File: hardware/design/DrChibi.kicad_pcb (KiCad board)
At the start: 4 copper layers, 143.5 x 14 mm, 255 parts, among them P1 CONN_02X05, P2 PAD_SMD, P3 IN+, P4 IN-, P5 CONN_01X04, U1 STM32F40X_LQFP64, U2 ISO1050, X1 MINI-USB-SHIELD-32005-201, X2 8MHz 10ppm

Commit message: Includex 4 fiducials for easier machine setup
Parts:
- removed REFSYMGNU: Symbol_GNU-Logo_SilkscreenTop, Symbols:Symbol_GNU-Logo_SilkscreenTop
- added REF**: Fiducial_1mm_Dia_2.54mm_Outer_CopperTop, Fiducials:Fiducial_1mm_Dia_2.54mm_Outer_CopperTop, F.Cu at (36.2, 98.1)
- added REF**: Fiducial_1mm_Dia_2.54mm_Outer_CopperTop, Fiducials:Fiducial_1mm_Dia_2.54mm_Outer_CopperTop, F.Cu at (176.4, 97.3)
- added REF**: Fiducial_1mm_Dia_2.54mm_Outer_CopperTop, Fiducials:Fiducial_1mm_Dia_2.54mm_Outer_CopperTop, F.Cu at (36.2, 101.7)
- added REF**: Fiducial_1mm_Dia_2.54mm_Outer_CopperTop, Fiducials:Fiducial_1mm_Dia_2.54mm_Outer_CopperTop, F.Cu at (176.4, 102.7)
- added REF**: Fiducial_1mm_Dia_2.54mm_Outer_CopperBottom, Fiducials:Fiducial_1mm_Dia_2.54mm_Outer_CopperBottom, F.Cu at (36.2, 98.1)
- added REF**: Fiducial_1mm_Dia_2.54mm_Outer_CopperBottom, Fiducials:Fiducial_1mm_Dia_2.54mm_Outer_CopperBottom, F.Cu at (36.2, 101.7)
- added REF**: Fiducial_1mm_Dia_2.54mm_Outer_CopperBottom, Fiducials:Fiducial_1mm_Dia_2.54mm_Outer_CopperBottom, F.Cu at (176.4, 97.3)
- added REF**: Fiducial_1mm_Dia_2.54mm_Outer_CopperBottom, Fiducials:Fiducial_1mm_Dia_2.54mm_Outer_CopperBottom, F.Cu at (176.4, 102.7)
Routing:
- net GND: track 948.4 -> 950.1 mm

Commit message: Included option for filtering sensev through small caps on RYSx
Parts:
- removed the REF** at (36.2, 98.1) (x2)
- removed the REF** at (176.4, 102.7) (x2)
- added RYSGND1: 0R/DNP, Resistors_SMD:R_0603_HandSoldering, B.Cu at (68.8, 101.3)
- moved REF** 1.78 mm to (36.2, 99.9) (x2)
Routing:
- net GND: track 950.1 -> 959.2 mm
- net /MCU/SENSVY2: track 13.3 -> 20.0 mm

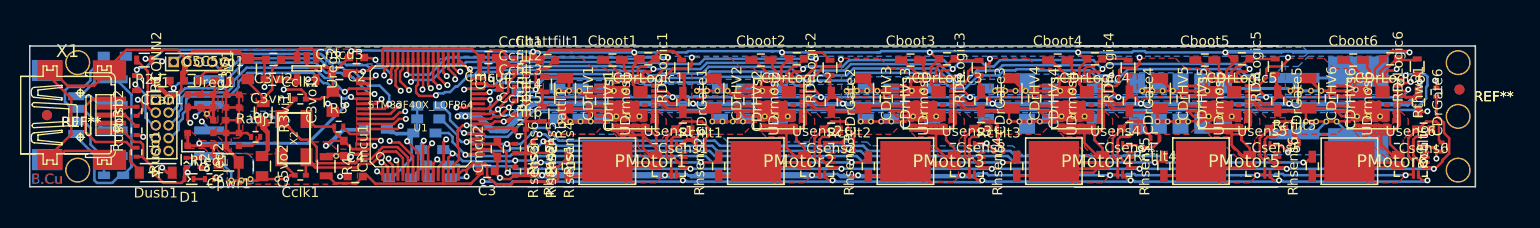
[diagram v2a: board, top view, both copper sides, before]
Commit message: Fixed footprint CDrHV1back6. Made a few things a little bit nicer.
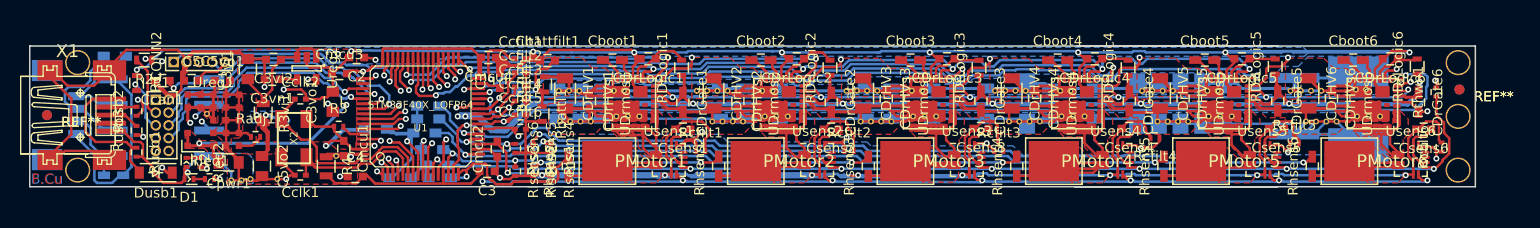
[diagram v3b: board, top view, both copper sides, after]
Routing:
- net GND: track 959.2 -> 1036.8 mm
- net +24V: track 240.0 -> 305.6 mm
- net /Half Bridge A/ZCD_EN: track 109.6 -> 110.8 mm
- net /Half Bridge D/PWM: track 71.5 -> 72.6 mm
- net /Half Bridge C/PWM: track 62.2 -> 63.1 mm
- net /Half Bridge E/PWM: track 84.1 -> 83.5 mm

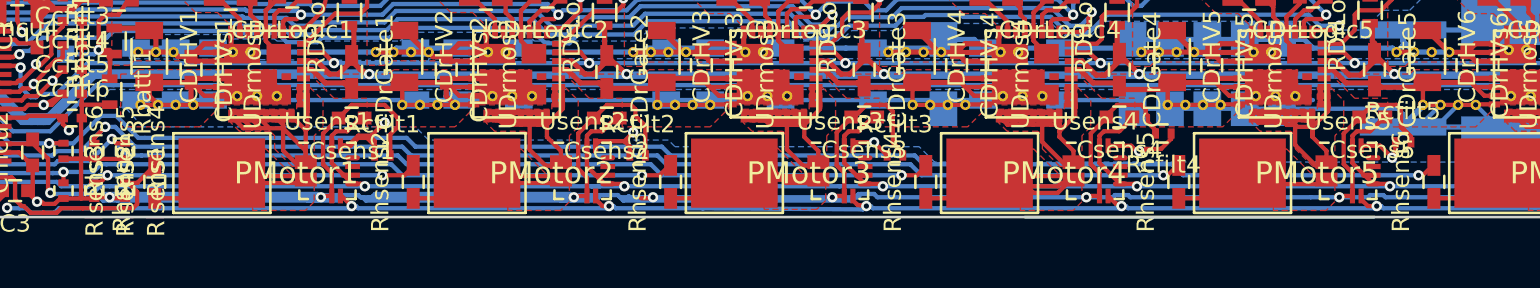
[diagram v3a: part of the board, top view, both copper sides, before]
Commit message: Added pads PVsensx for the application of alterate voltage sensing probes.
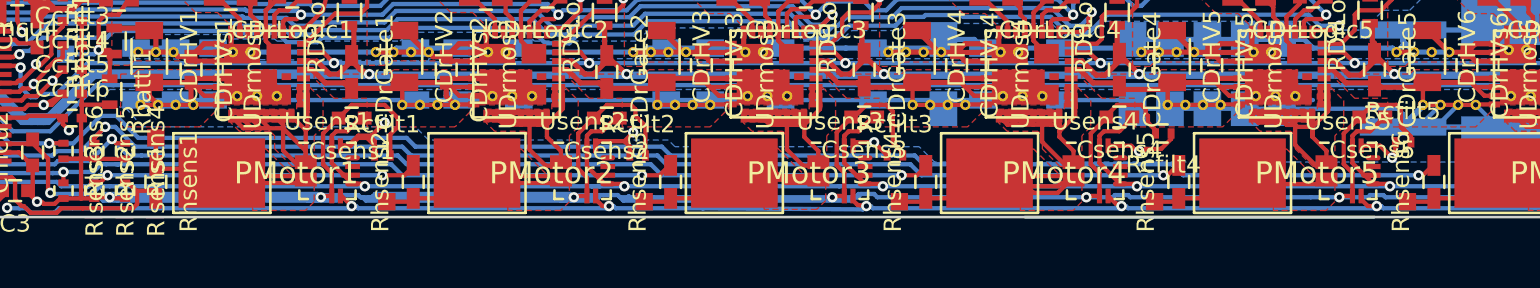
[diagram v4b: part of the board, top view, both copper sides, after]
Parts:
- added PVSens1: PAD_SMD, Pads:PAD_SMD_1x1, F.Cu at (88.0, 102.4)
- added PVSens2: PAD_SMD, Pads:PAD_SMD_1x1, F.Cu at (101.4, 106.1)
- added PVSens3: PAD_SMD, Pads:PAD_SMD_1x1, F.Cu at (116.2, 106.1)
- added PVSens4: PAD_SMD, Pads:PAD_SMD_1x1, F.Cu at (130.9, 106.1)
- added PVSens5: PAD_SMD, Pads:PAD_SMD_1x1, F.Cu at (145.7, 106.1)
- added PVSens6: PAD_SMD, Pads:PAD_SMD_1x1, F.Cu at (160.3, 106.1)
- moved Rhsens1 0.06 mm to (88.0, 105.0), turned to 270 degrees
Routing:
- net Net-(PMotor1-Pad1): track 16.9 -> 20.5 mm
- net Net-(PMotor4-Pad1): track 20.0 -> 21.6 mm
- net Net-(PMotor2-Pad1): track 14.8 -> 16.4 mm
- net Net-(PMotor3-Pad1): track 23.9 -> 25.5 mm
- net Net-(PMotor6-Pad1): track 14.3 -> 15.9 mm
- net Net-(PMotor5-Pad1): track 9.59 -> 11.1 mm
- net GND: track 1036.8 -> 1036.0 mm, vias 25 -> 24
- net /Virtual Y/SENS1: track 17.9 -> 17.2 mm

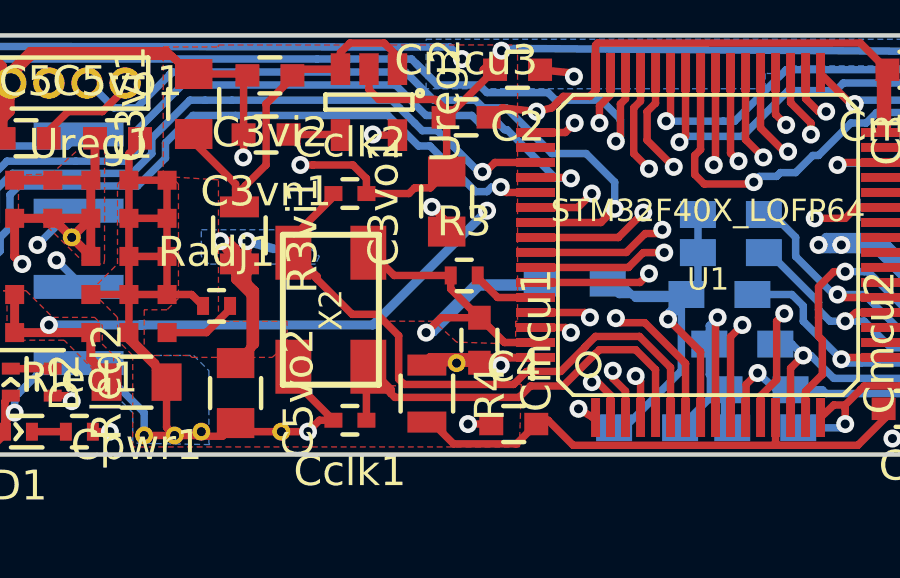
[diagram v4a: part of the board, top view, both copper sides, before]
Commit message: Added optional High Frequency AC-coupled voltage sensing port PHFAC
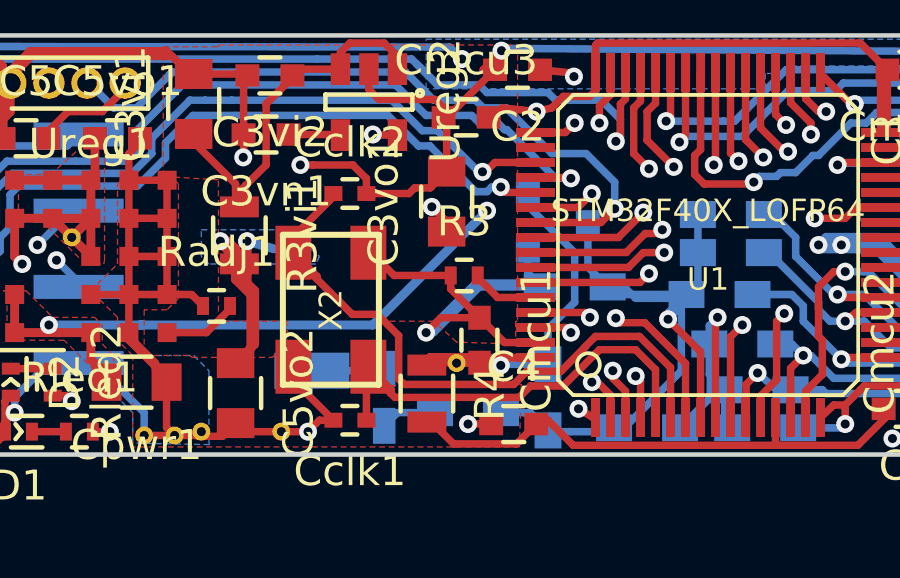
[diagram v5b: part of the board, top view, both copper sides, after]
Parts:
- added CHFAC1: C, Capacitors_SMD:C_0603_HandSoldering, B.Cu at (62.5, 105.1)
- added Dclamp1: D_Schottky_x2_Serial_AKC__BAT754S, TO_SOT_Packages_SMD:SOT-23, B.Cu at (68.3, 99.2)
- added PHFAC1: PAD_SMD, Pads:PAD_SMD_1.2x2.5, B.Cu at (60.1, 104.2)
- added RHFAC1: R, Resistors_SMD:R_0603_HandSoldering, B.Cu at (65.3, 105.6)
- added RYOFFS1: R, Resistors_SMD:R_0603_HandSoldering, B.Cu at (68.0, 105.1)
- moved RYSGND1 0.13 mm to (68.8, 101.4)
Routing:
- net +3V3: track 238.2 -> 246.5 mm
- net /MCU/SENSVY2: track 20.0 -> 26.5 mm
- net Net-(CHFAC1-Pad1): track 0.00 -> 2.44 mm
- net Net-(CHFAC1-Pad2): track 0.00 -> 1.88 mm
- net GND: track 1036.0 -> 1037.4 mm

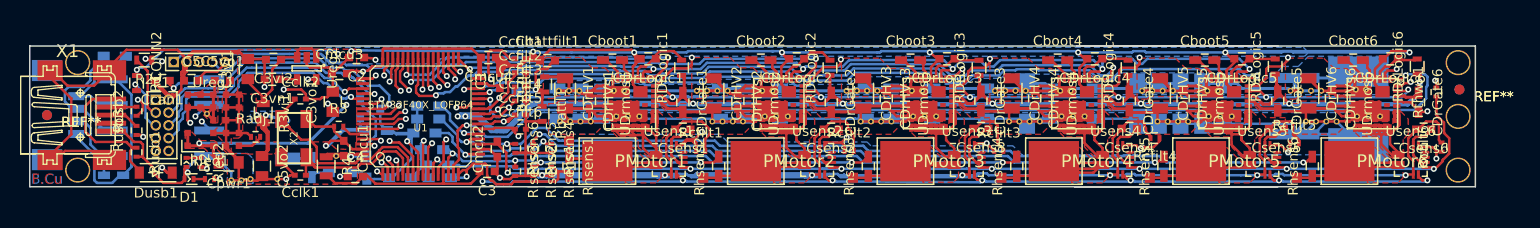
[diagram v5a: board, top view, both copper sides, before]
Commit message: Added pads for emergency bootloader execution.
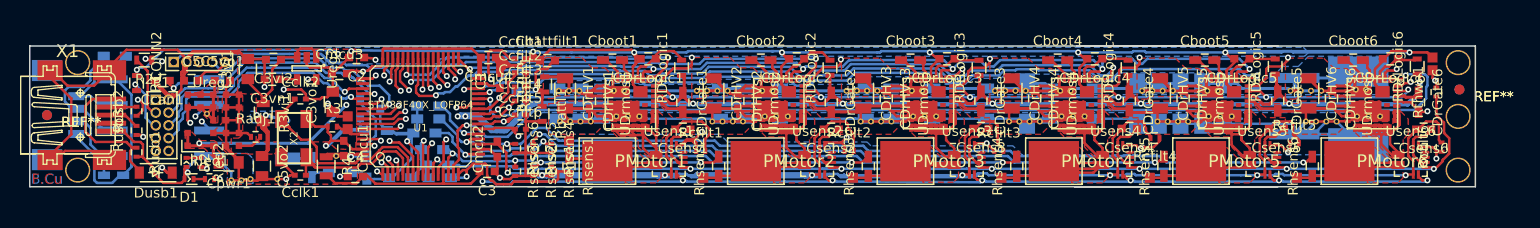
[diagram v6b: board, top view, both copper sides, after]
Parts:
- added PBOOT03V31: PAD_SMD, Pads:PAD_SMD_1x1, F.Cu at (66.1, 100.0)
- added PBOOT0P1: PAD_SMD, Pads:PAD_SMD_1x1, F.Cu at (66.1, 101.3)
- added PBOOT1GND1: PAD_SMD, Pads:PAD_SMD_1x1, F.Cu at (173.7, 94.2)
- added PBOOT1P1: PAD_SMD, Pads:PAD_SMD_1x1, F.Cu at (173.7, 95.4)
- Ccfilt1, Ccfilt2, Ccfilt3, Ccfilt4, Ccfilt5, Ccfilt6: value 0.5n -> 0.47n
- R3: value 2k7/DNP -> 2k2
- Rthwn1: value 2k7 -> 2k2
- moved REFSYMOSHW 59.9 mm to (82.4, 101.7)
- moved R3 0.64 mm to (64.5, 101.0)
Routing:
- net +3V3: track 246.5 -> 248.1 mm
- net GND: track 1037.4 -> 1039.0 mm
- net Net-(PBOOT0P1-Pad1): track 2.18 -> 3.66 mm
- net /Half Bridge A/THWn: track 110.2 -> 111.3 mm

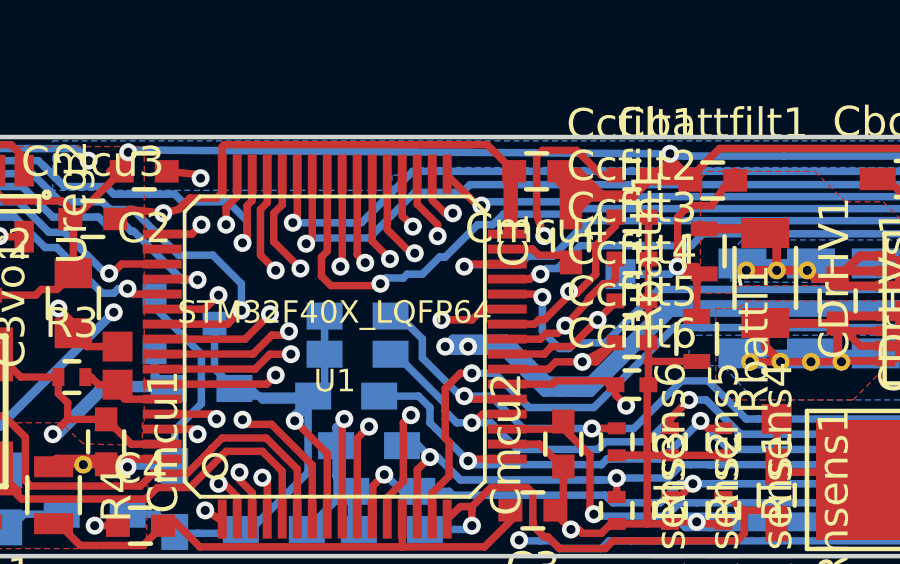
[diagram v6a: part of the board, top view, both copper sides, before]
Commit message: TODO Double-check BOM. Check silk screen. Check Gerber output.
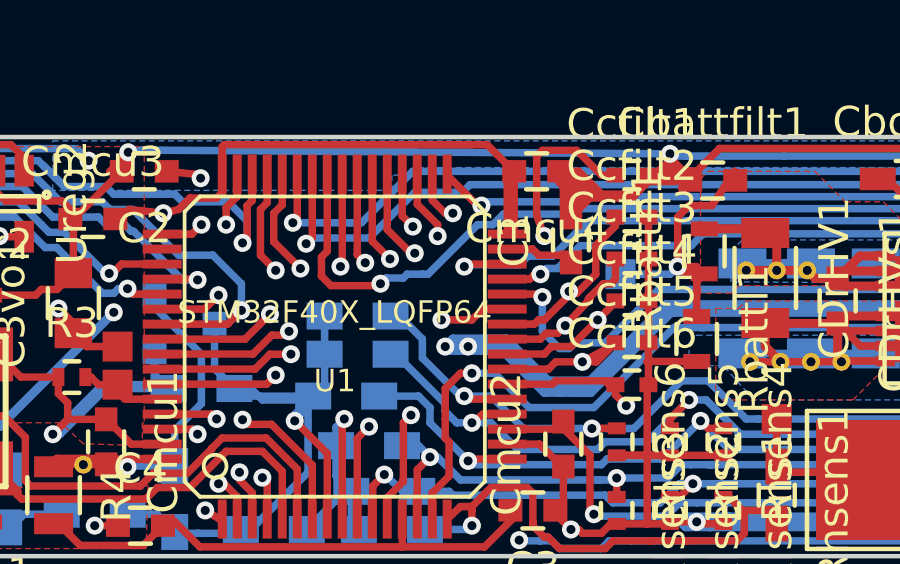
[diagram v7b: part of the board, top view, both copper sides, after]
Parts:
- CDrHV1, CDrHV2, CDrHV3, CDrHV4, CDrHV5, CDrHV6: value 10u -> 10u,35V
- CDrHV1back1, CDrHV1back2, CDrHV1back3, CDrHV1back4, CDrHV1back5, CDrHV1back6: value 4.7u -> 4.7u,35V
- CDrHV2back1, CDrHV2back2, CDrHV2back3, CDrHV2back4, CDrHV2back5, CDrHV2back6: value 4.7u -> 10u,35V
- CDrHVs1, CDrHVs2, CDrHVs3, CDrHVs4, CDrHVs5, CDrHVs6: value 0.47u -> 0.47u,35V
- CHFAC1: value C -> 10n
- Cclk1, Cclk2: value 15p -> 18p
- R1, R2: value 100 -> 100R
- RDrLogic1, RDrLogic2, RDrLogic3, RDrLogic4, RDrLogic5, RDrLogic6, RHFAC1: value R -> 100R
- RYOFFS1: value R -> 20k
- RYSGND1: value 0R/DNP -> 20k
- Rhsens1, Rhsens2, Rhsens3, Rhsens4, Rhsens5, Rhsens6: value 10k -> 10k,0.1%
- Rlsens1, Rlsens2, Rlsens3, Rlsens4, Rlsens5, Rlsens6: value 2k2 -> 2k2,0.1%

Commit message: Added just a few words...
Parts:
- CHFAC1: value 10n -> 10n,35V
- moved G*** 1.92 mm to (61.7, 98.4)
- moved REFSYMOSHW 0.88 mm to (83.1, 101.0)
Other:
- board text added: "APARAZZI"
- board text added: "BLDC"
- board text added: "DrChibi, Looong-Strip"
- board text added: "F R E E hardware design"
- board text added: "P"
- board text added: "PHFAC1"
- board text added: "PMSM"
- board text added: "Power for"
- board text added: "Stepper"
- board text added: "flight for peace"
- board text added: "no cry"
- board text added: "no sensors"
- board text added: "stronger"
- board text removed: "Looong-Strip"
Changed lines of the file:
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@@
     (area 34.424999 92.939999 178.075001 107.060001)
     (thickness 1.6)
-    (drawings 31)
+    (drawings 43)
     (tracks 3765)
     (zones 0)
@@
     (pcbplotparams
       (layerselection 0x00030_ffffffff)
-      (usegerberextensions false)
+      (usegerberextensions true)
       (excludeedgelayer true)
       (linewidth 0.100000)
@@
       (psnegative false)
       (psa4output false)
-      (plotreference true)
-      (plotvalue true)
+      (plotreference false)
+      (plotvalue false)
       (plotinvisibletext false)
       (padsonsilk false)
@@
       (outputformat 1)
       (mirror false)
-      (drillshape 1)
+      (drillshape 0)
       (scaleselection 1)
-      (outputdirectory ""))
+      (outputdirectory fab/))
   )
   (net 0 "")
@@
   )
   (module Symbols:Symbol_OSHW-Logo_SilkScreen (layer B.Cu)
-    (at 82.436 101.651 180)
+    (at 83.071 101.0414 180)
     (descr "Symbol, OSHW-Logo, Silk Screen,")
     (tags "Symbol, OSHW-Logo, Silk Screen,")
@@
   )
   (module Symbols_User:CERN_OHL (layer B.Cu)
-    (at 60.338 99.746 180)
+    (at 61.735 98.4252 180)
     (fp_text reference G*** (at 0 0 180) (layer B.SilkS) hide
       (effects (font (thickness 0.3)) (justify mirror))
@@
       (effects (font (size 1 1) (thickness 0.15)) (justify mirror))
     )
-    (fp_text value 10n (at 0 -1.9 270) (layer B.Fab)
+    (fp_text value 10n,35V (at 0 -1.9 270) (layer B.Fab)
       (effects (font (size 1 1) (thickness 0.15)) (justify mirror))
     )
@@
       (net 4 +3V3))
   )
+  (gr_text "F R E E\nhardware design" (at 73.4444 95.5804) (layer B.SilkS)
+    (effects (font (size 1 1) (thickness 0.25)) (justify mirror))
+  )
+  (gr_text stronger (at 137.808 105.334) (layer B.SilkS)
+    (effects (font (size 0.9 0.9) (thickness 0.2)) (justify mirror))
+  )
+  (gr_text Stepper (at 137.808 103.937) (layer B.SilkS)
+    (effects (font (size 0.9 1) (thickness 0.2)) (justify mirror))
+  )
+  (gr_text "no cry" (at 145.1486 105.2832) (layer B.SilkS)
+    (effects (font (size 0.9 0.9) (thickness 0.2)) (justify mirror))
+  )
+  (gr_text BLDC (at 151.2954 105.334) (layer B.SilkS)
+    (effects (font (size 0.9 0.9) (thickness 0.2)) (justify mirror))
+  )
+  (gr_text PMSM (at 151.27 103.9624) (layer B.SilkS)
+    (effects (font (size 0.9 0.8) (thickness 0.2)) (justify mirror))
+  )
+  (gr_text "Power for" (at 158.3058 104.572) (layer B.SilkS)
+    (effects (font (size 2.4 1.2) (thickness 0.25)) (justify mirror))
+  )
+  (gr_text "no sensors" (at 144.9962 103.9116) (layer B.SilkS)
+    (effects (font (size 0.9 0.8) (thickness 0.2)) (justify mirror))
+  )
+  (gr_text P (at 133.0836 104.064) (layer B.SilkS)
+    (effects (font (size 1 1.4) (thickness 0.25)) (justify mirror))
+  )
+  (gr_text "flight for peace" (at 128.918 105.3848) (layer B.SilkS)
+    (effects (font (size 0.8 0.8) (thickness 0.2)) (justify mirror))
+  )
+  (gr_text APARAZZI (at 128.3084 104.191) (layer B.SilkS)
+    (effects (font (size 0.8 1.2) (thickness 0.2)) (justify mirror))
+  )
+  (gr_text PHFAC1 (at 58.6108 105.8166) (layer B.SilkS)
+    (effects (font (size 1 1) (thickness 0.25)) (justify mirror))
+  )
   (gr_text 6 (at 76.2384 98.984) (layer B.SilkS)
     (effects (font (size 0.8 0.8) (thickness 0.2)) (justify mirror))
@@
     (effects (font (size 1 1) (thickness 0.25)) (justify mirror))
   )
-  (gr_text Rcan (at 46.5204 94.0564) (layer B.SilkS)
+  (gr_text Rcan (at 46.4188 94.0818) (layer B.SilkS)
     (effects (font (size 1 1) (thickness 0.25)) (justify mirror))
   )
@@
     (effects (font (size 1.5 1.5) (thickness 0.3)) (justify mirror))
   )
-  (gr_text "CERN OHL" (at 60.211 105.842) (layer B.SilkS)
-    (effects (font (size 1 1.5) (thickness 0.25)) (justify mirror))
+  (gr_text "CERN OHL" (at 56.6804 98.5014 90) (layer B.SilkS)
+    (effects (font (size 1 1.3) (thickness 0.25)) (justify mirror))
   )
-  (gr_text CC-BY-SA (at 76.848 97.333) (layer B.SilkS)
-    (effects (font (size 1 1) (thickness 0.25)) (justify mirror))
+  (gr_text CC-BY-SA (at 79.0578 101.8034 90) (layer B.SilkS)
+    (effects (font (size 0.9 0.9) (thickness 0.2)) (justify mirror))
   )
-  (gr_text Looong-Strip (at 82.563 94.793) (layer B.SilkS)
-    (effects (font (size 2 2) (thickness 0.25)) (justify mirror))
+  (gr_text "DrChibi, Looong-Strip" (at 105.7024 94.8946) (layer B.SilkS)
+    (effects (font (size 2 2) (thickness 0.3)) (justify mirror))
   )
-  (gr_text github.com/joewa/ChibiESC (at 108.217 104.826) (layer B.SilkS)
+  (gr_text github.com/joewa/ChibiESC (at 105.8548 104.6482) (layer B.SilkS)
     (effects (font (size 1.5 1.5) (thickness 0.25)) (justify mirror))
   )
